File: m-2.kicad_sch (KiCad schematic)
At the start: 50 parts, among them J301 1-2199230-6, J302 2199230-6, M1 M2_4222, M301 M2_2280, U301 74LVC2G07GV, U302 74LVC2G07GV

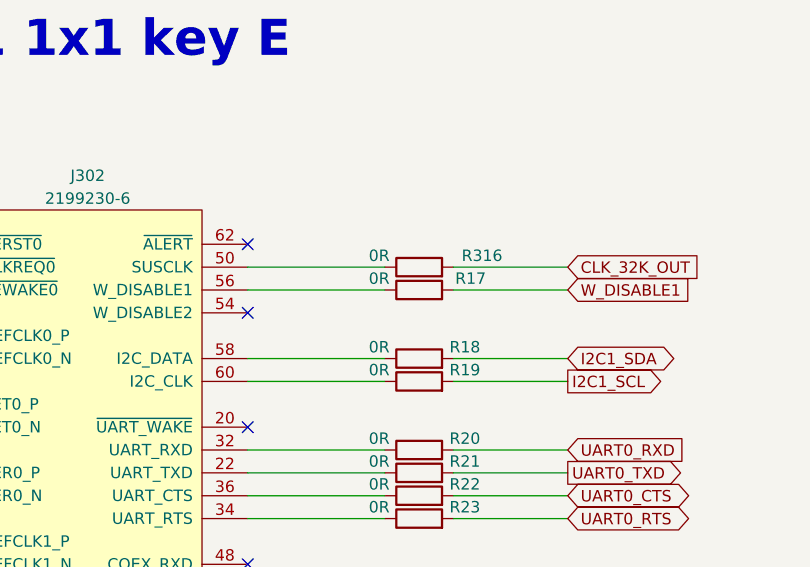
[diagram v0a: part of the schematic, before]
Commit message: Connect W_DISABLE2 to SoM GPIO via RO
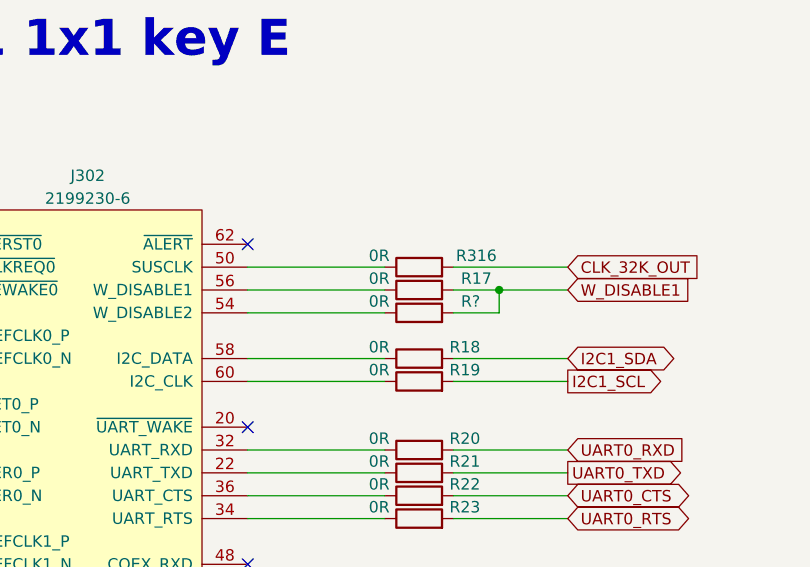
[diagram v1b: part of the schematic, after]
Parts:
- added R?: R_0R_0402, antmicro-footprints:0402-res, symbol antmicroResistors0402:R_0R_0402
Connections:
- net W_DISABLE1: now also R?.2
- net at J302.54 (W_DISABLE2): now also R?.1
- no-connect marks 31 -> 30
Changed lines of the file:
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@@
   (junction (at 294.64 33.02) (diameter 0) (color 0 0 0 0)
   )
+  (junction (at 257.81 166.37) (diameter 0) (color 0 0 0 0)
+  )
   (junction (at 345.44 66.04) (diameter 0) (color 0 0 0 0)
   )
@@
   (no_connect (at 229.87 228.6))
   (no_connect (at 229.87 231.14))
-  (no_connect (at 229.87 168.91))
   (no_connect (at 229.87 181.61))
   (no_connect (at 229.87 199.39))
@@
     (stroke (width 0) (type default) (color 0 0 0 0))
   )
-  (wire (pts (xy 252.73 166.37) (xy 265.43 166.37))
+  (wire (pts (xy 252.73 166.37) (xy 257.81 166.37))
     (stroke (width 0) (type default) (color 0 0 0 0))
   )
@@
     (stroke (width 0) (type default) (color 0 0 0 0))
   )
+  (wire (pts (xy 252.73 168.91) (xy 257.81 168.91))
+    (stroke (width 0) (type default) (color 0 0 0 0))
+  )
   (wire (pts (xy 345.44 100.33) (xy 345.44 102.87))
     (stroke (width 0) (type default) (color 0 0 0 0))
   )
+  (wire (pts (xy 257.81 166.37) (xy 265.43 166.37))
+    (stroke (width 0) (type default) (color 0 0 0 0))
+  )
   (wire (pts (xy 52.07 104.14) (xy 62.23 104.14))
     (stroke (width 0) (type default) (color 0 0 0 0))
@@
     (stroke (width 0) (type default) (color 0 0 0 0))
   )
+  (wire (pts (xy 257.81 168.91) (xy 257.81 166.37))
+    (stroke (width 0) (type default) (color 0 0 0 0))
+  )
   (wire (pts (xy 289.56 22.86) (xy 294.64 22.86))
     (stroke (width 0) (type default) (color 0 0 0 0))
@@
     (stroke (width 0) (type default) (color 0 0 0 0))
   )
+  (wire (pts (xy 229.87 168.91) (xy 245.11 168.91))
+    (stroke (width 0) (type default) (color 0 0 0 0))
+  )
   (wire (pts (xy 147.32 50.8) (xy 147.32 63.5))
     (stroke (width 0) (type default) (color 0 0 0 0))
@@
   (symbol (lib_id "antmicroResistors0402:R_0R_0402") (at 248.92 163.83 0) (unit 1)
     (in_bom yes) (on_board yes)
-    (property "Reference" "R316" (id 0) (at 255.905 162.56 0))
+    (property "Reference" "R316" (id 0) (at 255.27 162.56 0))
     (property "Value" "R_0R_0402" (id 1) (at 248.92 167.64 0)
       (effects (font (size 1.27 1.27)) hide)
@@
     (pin "2")
   )
+  (symbol (lib_id "antmicroResistors0402:R_0R_0402") (at 248.92 168.91 0) (unit 1)
+    (in_bom yes) (on_board yes)
+    (property "Reference" "R?" (id 0) (at 254.635 167.64 0))
+    (property "Value" "R_0R_0402" (id 1) (at 248.92 172.72 0)
+      (effects (font (size 1.27 1.27)) hide)
+    )
+    (property "Footprint" "antmicro-footprints:0402-res" (id 2) (at 254 163.83 0)
+      (effects (font (size 1.524 1.524)) (justify left) hide)
+    )
+    (property "Datasheet" "" (id 3) (at 248.92 168.91 0)
+      (effects (font (size 1.27 1.27)) hide)
+    )
+    (property "Manufacturer" "PANASONIC" (id 4) (at 254 158.75 0)
+      (effects (font (size 1.524 1.524)) (justify left) hide)
+    )
+    (property "MPN" "ERJ2GE0R00X" (id 5) (at 254 161.29 0)
+      (effects (font (size 1.524 1.524)) (justify left) hide)
+    )
+    (property "Val" "0R" (id 6) (at 244.475 167.64 0))
+    (pin "1")
+    (pin "2")
+  )
   (symbol (lib_id "antmicroCapacitors0603:C_10u_0603") (at 368.3 51.435 0) (mirror y) (unit 1)
     (in_bom yes) (on_board yes) (fields_autoplaced)
@@
   (symbol (lib_id "antmicroResistors0402:R_0R_0402") (at 248.92 166.37 0) (unit 1)
     (in_bom yes) (on_board yes)
-    (property "Reference" "R17" (id 0) (at 254.635 165.1 0))
+    (property "Reference" "R17" (id 0) (at 255.27 165.1 0))
     (property "Value" "R_0R_0402" (id 1) (at 248.92 170.18 0)
       (effects (font (size 1.27 1.27)) hide)

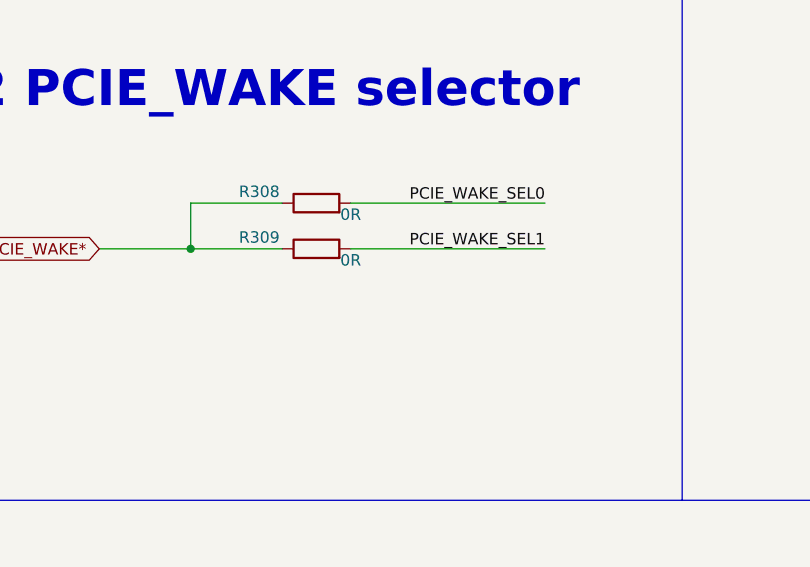
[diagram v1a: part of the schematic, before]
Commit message: Add connection between M.2 Wake selector and expander connector
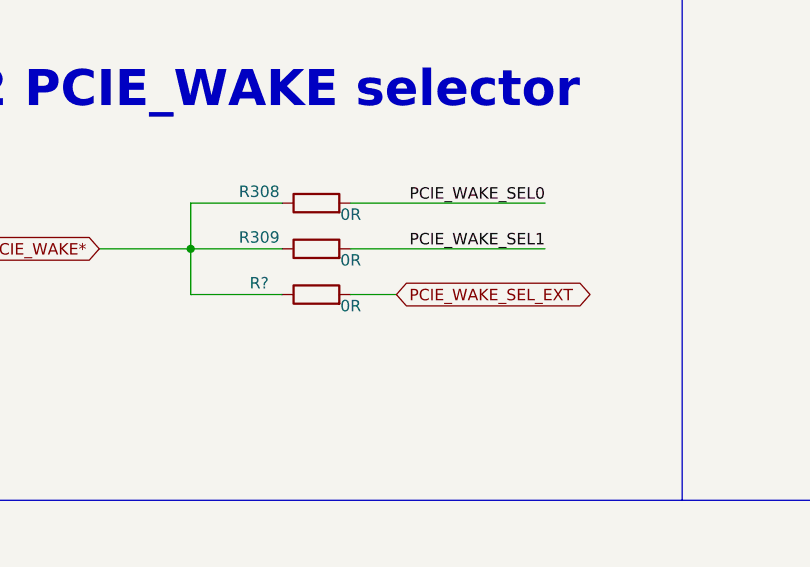
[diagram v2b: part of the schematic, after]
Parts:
- added R?: R_0R_0402, antmicro-footprints:0402-res, symbol antmicroResistors0402:R_0R_0402
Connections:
- net PCIE_WAKE*: now also R?.1
- new net PCIE_WAKE_SEL_EXT: R?.2
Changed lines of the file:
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@@
     (stroke (width 0) (type default) (color 0 0 0 0))
   )
+  (wire (pts (xy 52.07 104.14) (xy 52.07 109.22))
+    (stroke (width 0) (type default) (color 0 0 0 0))
+  )
   (wire (pts (xy 271.145 87.63) (xy 267.97 87.63))
     (stroke (width 0) (type default) (color 0 0 0 0))
@@
     (stroke (width 0) (type default) (color 0 0 0 0))
   )
+  (wire (pts (xy 69.85 109.22) (xy 74.93 109.22))
+    (stroke (width 0) (type default) (color 0 0 0 0))
+  )
   (wire (pts (xy 345.44 120.65) (xy 345.44 123.19))
     (stroke (width 0) (type default) (color 0 0 0 0))
@@
     (stroke (width 0) (type default) (color 0 0 0 0))
   )
+  (wire (pts (xy 52.07 109.22) (xy 62.23 109.22))
+    (stroke (width 0) (type default) (color 0 0 0 0))
+  )
   (wire (pts (xy 147.32 76.2) (xy 147.32 63.5))
     (stroke (width 0) (type default) (color 0 0 0 0))
@@
     )
   )
+  (global_label "PCIE_WAKE_SEL_EXT" (shape bidirectional) (at 74.93 109.22 0)
+    (effects (font (size 1.27 1.27)) (justify left))
+    (property "Intersheet References" "${INTERSHEET_REFS}" (id 0) (at 97.79 109.22 0)
+      (effects (font (size 1.27 1.27)) (justify left))
+    )
+  )
   (global_label "PCIE0_RX1_P" (shape bidirectional) (at 267.97 80.01 180)
     (effects (font (size 1.27 1.27)) (justify right))
@@
     (pin "1")
   )
+  (symbol (lib_id "antmicroResistors0402:R_0R_0402") (at 66.04 109.22 0) (unit 1)
+    (in_bom yes) (on_board yes)
+    (property "Reference" "R?" (id 0) (at 59.69 107.95 0))
+    (property "Value" "R_0R_0402" (id 1) (at 66.04 113.03 0)
+      (effects (font (size 1.27 1.27)) hide)
+    )
+    (property "Footprint" "antmicro-footprints:0402-res" (id 2) (at 71.12 104.14 0)
+      (effects (font (size 1.524 1.524)) (justify left) hide)
+    )
+    (property "Datasheet" "" (id 3) (at 66.04 109.22 0)
+      (effects (font (size 1.27 1.27)) hide)
+    )
+    (property "Manufacturer" "PANASONIC" (id 4) (at 71.12 99.06 0)
+      (effects (font (size 1.524 1.524)) (justify left) hide)
+    )
+    (property "MPN" "ERJ2GE0R00X" (id 5) (at 71.12 101.6 0)
+      (effects (font (size 1.524 1.524)) (justify left) hide)
+    )
+    (property "Val" "0R" (id 6) (at 69.85 110.49 0))
+    (pin "1")
+    (pin "2")
+  )
   (symbol (lib_id "power:GND") (at 391.795 120.65 0) (unit 1)

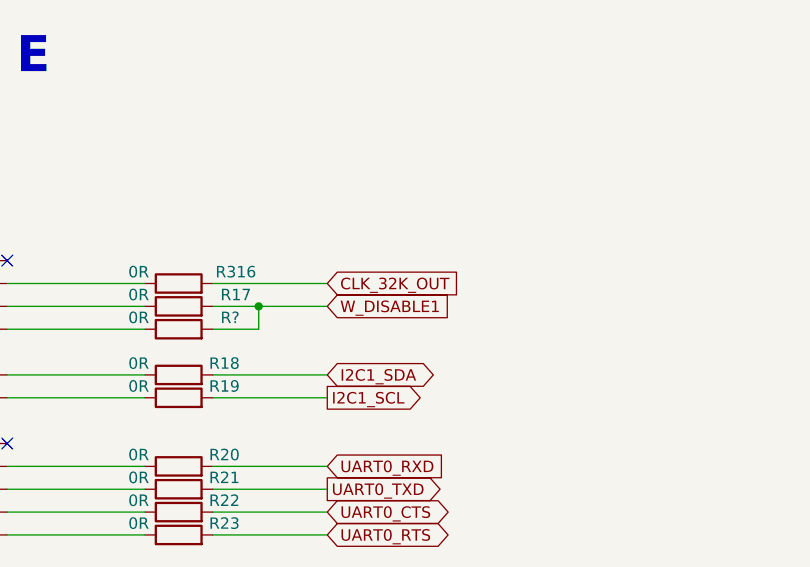
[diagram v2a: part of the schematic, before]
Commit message: Add 3V3 translator to 32kHz clock
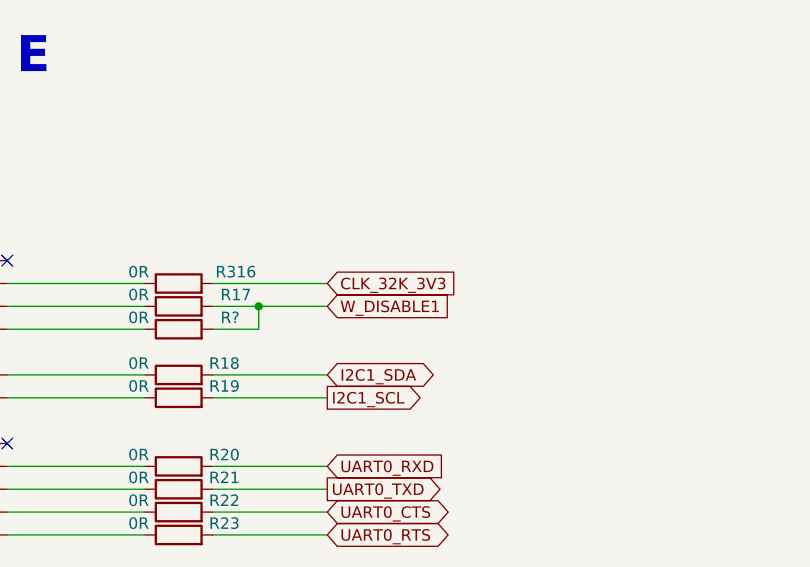
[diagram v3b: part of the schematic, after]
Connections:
- net CLK_32K_OUT: no longer R316.2
- new net CLK_32K_3V3: R316.2
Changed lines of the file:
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@@
-    )
-  )
-  (global_label "CLK_32K_OUT" (shape input) (at 265.43 163.83 0) (fields_autoplaced)
-    (effects (font (size 1.27 1.27)) (justify left))
-    (property "Intersheet References" "${INTERSHEET_REFS}" (id 0) (at 280.6641 163.7506 0)
-      (effects (font (size 1.27 1.27)) (justify left))
     )
   )
@@
       (effects (font (size 1.27 1.27)) (justify left))
     )
+  )
+  (global_label "CLK_32K_3V3" (shape input) (at 265.43 163.83 0) (fields_autoplaced)
+    (effects (font (size 1.27 1.27)) (justify left))
+    (property "Intersheet References" "${INTERSHEET_REFS}" (id 0) (at 280.5431 163.9094 0)
+      (effects (font (size 1.27 1.27)) (justify left))
+    )

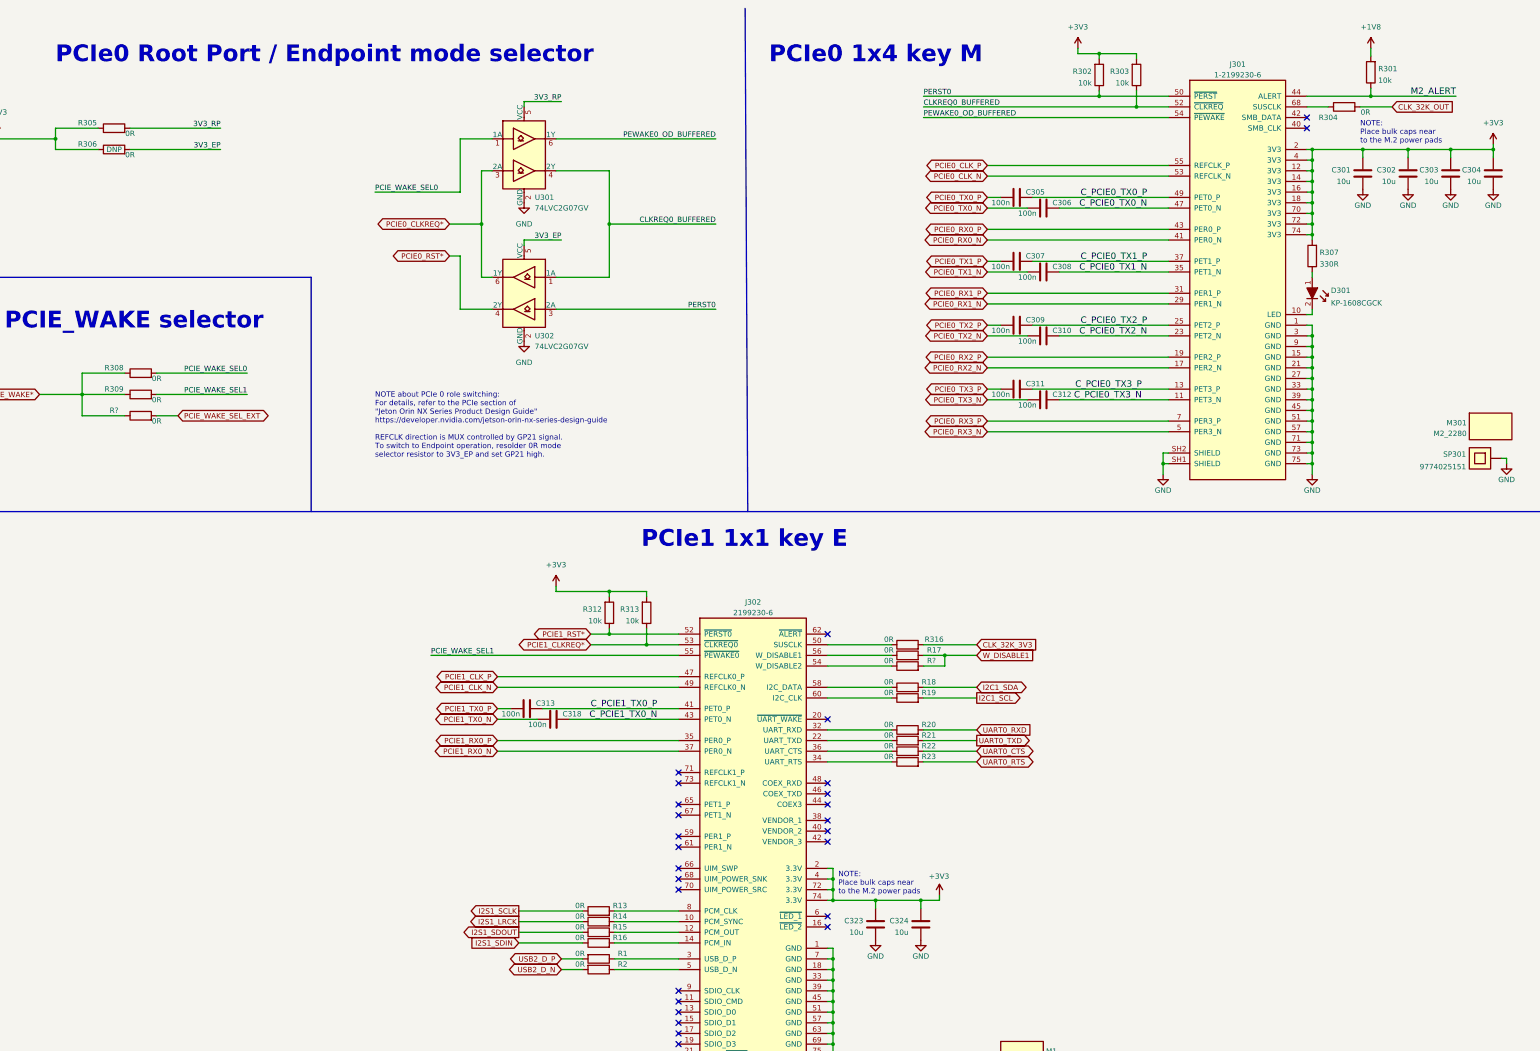
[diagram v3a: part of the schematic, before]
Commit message: Add labels to M.2 key E signals
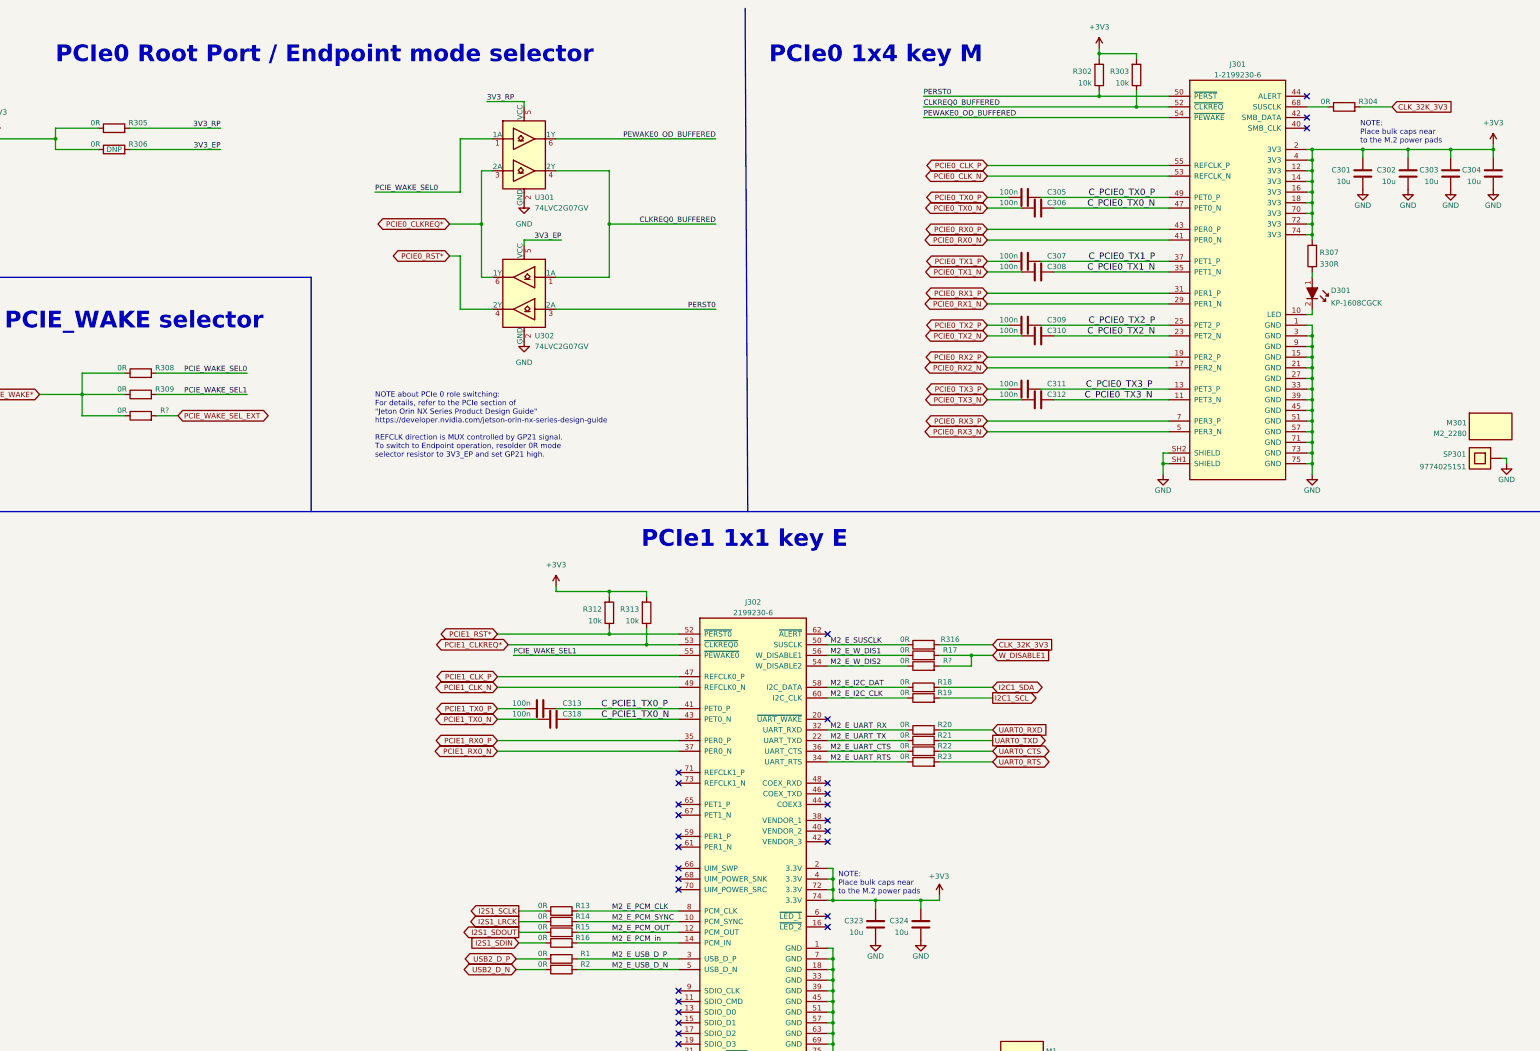
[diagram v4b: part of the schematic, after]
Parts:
- removed R301: R_10k_0402, antmicro-footprints:0402-res, symbol antmicroResistors0402:R_10k_0402
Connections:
- net CLK_32K_OUT is gone; now on net CLK_32K_3V3: R304.2
- net M2_E_USB_D_P: now reaches J302.3 (USB_D_P), R1.1
- net M2_E_UART_RTS: now reaches J302.34 (UART_RTS), R23.1
- net M2_E_I2C_DAT: now reaches J302.58 (I2C_DATA), R18.1
- net M2_E_PCM_SYNC: now reaches J302.10 (PCM_SYNC), R14.2
- net M2_E_USB_D_N: now reaches J302.5 (USB_D_N), R2.1
- net M2_E_PCM_OUT: now reaches J302.12 (PCM_OUT), R15.2
- net M2_E_PCM_in: now reaches J302.14 (PCM_IN), R16.2
- net M2_E_UART_TX: now reaches J302.22 (UART_TXD), R21.1
- net M2_E_UART_RX: now reaches J302.32 (UART_RXD), R20.1
- net M2_E_UART_CTS: now reaches J302.36 (UART_CTS), R22.1
- net M2_E_SUSCLK: now reaches J302.50 (SUSCLK), R316.1
- net M2_E_W_DIS2: now reaches J302.54 (W_DISABLE2), R?.1
- net M2_E_W_DIS1: now reaches J302.56 (W_DISABLE1), R17.1
- net M2_E_I2C_CLK: now reaches J302.60 (I2C_CLK), R19.1
- net M2_E_PCM_CLK: now reaches J302.8 (PCM_CLK), R13.2
- net M2_ALERT: no longer names the net of J301.44 (ALERT)
- no-connect marks 30 -> 31
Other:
- moved on the sheet: C305, C306, C307, C308, C309, C310, C311, C312, C313, R1, R13, R14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

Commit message: Add 32.7kHz oscillator to M2 key M
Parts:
- removed R302, R303, R312, R313: R_10k_0402, antmicro-footprints:0402-res, symbol antmicroResistors0402:R_10k_0402
- removed R304: R_0R_0402, antmicro-footprints:0402-res, symbol antmicroResistors0402:R_0R_0402
- added C?: C_100n_0402, antmicro-footprints:0402-cap, symbol antmicroCapacitors0402:C_100n_0402
- added R? (x5): R_47k_0402, antmicro-footprints:0402-res, symbol antmicroResistors0402:R_47k_0402
- added R? (x2): R_0R_0402, antmicro-footprints:0402-res, symbol antmicroResistors0402:R_0R_0402
- added TP? (x3): TP_SMD_0_75MM, antmicro-footprints:Testpoint_smd_0_75mm, symbol antmicroTestPoints:TP_SMD_0_75MM
- added Y?: ECS-327MVATX-2-CN-TR3, antmicro-footprints:Oscillator_SMD_ECS_2520MV-xxx-xx-4Pin_2.5x2.0mm, symbol antmicroOscillators:ECS-327MVATX-2-CN-TR3
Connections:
- net +3V3: now also C?.1, R?.1, R?.1, R?.1, R?.1, R?.2, Y?.1 (EN), Y?.4 (VDD)
- net CLKREQ0_BUFFERED: now also R?.2
- net GND: now also C?.2, Y?.2 (GND)
- net PCIE1_CLKREQ*: now also R?.2
- net PCIE1_RST*: now also R?.2
- net PERST0: now also R?.2
- net UART0_RXD: now also R21.2; no longer R20.2
- net UART0_TXD: now also R20.2; no longer R21.2
- net ~{M2_E_UART_WAKE}: now reaches J302.20 (~{UART_WAKE})
- net ~{M2_E_UART_WAKE}: now also R?.1, R?.1
- net ~{M2_E_ALERT}: now reaches J302.62 (~{ALERT})
- net ~{M2_E_ALERT}: now also R?.1
- net M2_M_SUSCLK: now reaches J301.68 (SUSCLK)
- net M2_M_SUSCLK: now also Y?.3 (OUT)
- net at J301.40 (SMB_CLK): now also TP?.1
- net at J301.42 (SMB_DATA): now also TP?.1
- net ~{M2_M_ALERT}: now reaches J301.44 (ALERT)
- net ~{M2_M_ALERT}: now also TP?.1
- net W_DISABLE1 renamed SoM_GPIO_xxx
- net SoM_GPIO_xxx: now also R?.2, R?.2
- no-connect marks 31 -> 26
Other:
- moved on the sheet: R17, R18, R19, R20, R21, R22, R23, R316, R?
